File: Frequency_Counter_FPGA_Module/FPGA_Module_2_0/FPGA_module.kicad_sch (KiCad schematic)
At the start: 0 parts

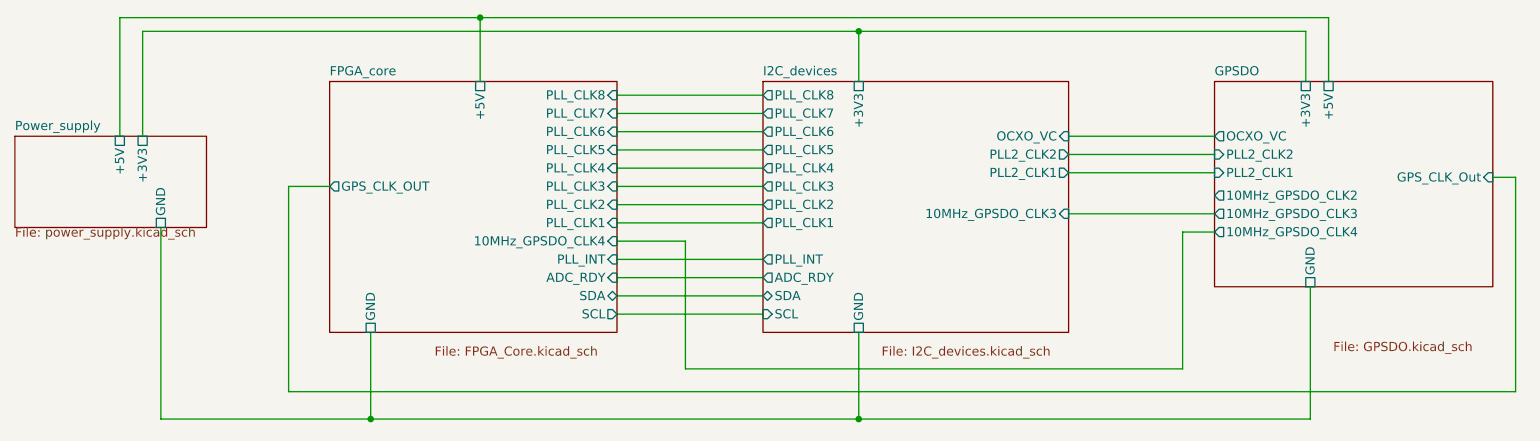
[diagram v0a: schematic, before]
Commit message: feat(boot): LED selftest blikaci kod + RTC LSE medium-low drive; UI 4.3" audit; FPGA HW revize
STM32H757 firmware:
- bootled.c/h: boot-time HW selftest diagnostika na LED_1 (PG3). Kazdy
  sledovany periferni init (FMC/SPI2/I2C4/DSIHOST/LTDC/USART1/RTC/ADC3/
  QUADSPI/I2C1) + display bring-up (panel probe/power-on/DSI start/
  TC358762) si zaznamena poradove cislo; pri zaseknuti v Error_Handler()
  LED bez displeje zabliká N-krat podle poradi. Regen-safe (jen chranene
  USER CODE hooky), bez zpozdeni v happy-path.
- RTC LSE Drive Capability LOW -> MEDIUM LOW (H757_LED.ioc): kompenzuje
  desky s predimenzovanymi zatezovymi kondenzatory krystalu (22pF misto
  18pF), ktere LSE nerozjizdely.
- UI audit pro realny 4,3" 800x480 panel (8,54 px/mm): hit-slop pilulek,
  fonty, HDR_PILL_LIMIT fit-check, Menu 3x4 mrizka s placeholdery, oprava
  ghost bugu AUTO CET/CEST tlacitka, sign-loss bug ve fmt_fixed/fmt_minmax.
  main-old layout zamrazen jako default (A/B srovnani, viz STATUS.md #14).

FPGA carrier v2.0 (KiCad): prubezne review checklisty a schema/PCB revize.

Co-Authored-By: OK2JNJ <ok2jnj@local>
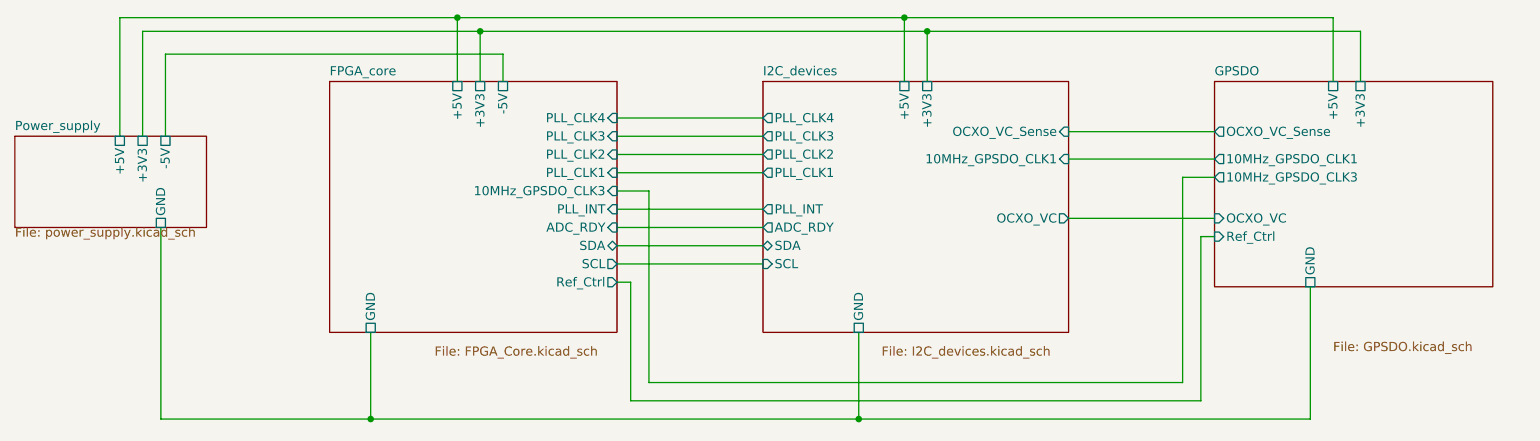
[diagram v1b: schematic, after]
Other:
- sheet FPGA_core ports: added +3V3, -5V, 10MHz_GPSDO_CLK3, Ref_Ctrl; removed 10MHz_GPSDO_CLK4, GPS_CLK_OUT, PLL_CLK5, PLL_CLK6, PLL_CLK7, PLL_CLK8
- sheet GPSDO ports: added 10MHz_GPSDO_CLK1, OCXO_VC_Sense, Ref_Ctrl; removed 10MHz_GPSDO_CLK2, 10MHz_GPSDO_CLK4, GPS_CLK_Out, PLL2_CLK1, PLL2_CLK2
- sheet I2C_devices ports: added +5V, 10MHz_GPSDO_CLK1, OCXO_VC_Sense; removed 10MHz_GPSDO_CLK3, PLL2_CLK1, PLL2_CLK2, PLL_CLK5, PLL_CLK6, PLL_CLK7, PLL_CLK8
- sheet Power_supply ports: added -5V; removed none

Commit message: feat(hw): FPGA carrier v2.0 — aktualizace schematu + PCB + checklist
KiCad FPGA_Module_2_0 (FPGA_Core/GPSDO/I2C_devices/power_supply schemata,
PCB layout, project), BOARD_V20_CHECKLIST.md. Odstranen zastaraly
FPGA_module_schematic.pdf (nahrazen exportem FPGA_module.pdf).

Co-Authored-By: OK2JNJ <ok2jnj@users.noreply.github.com>
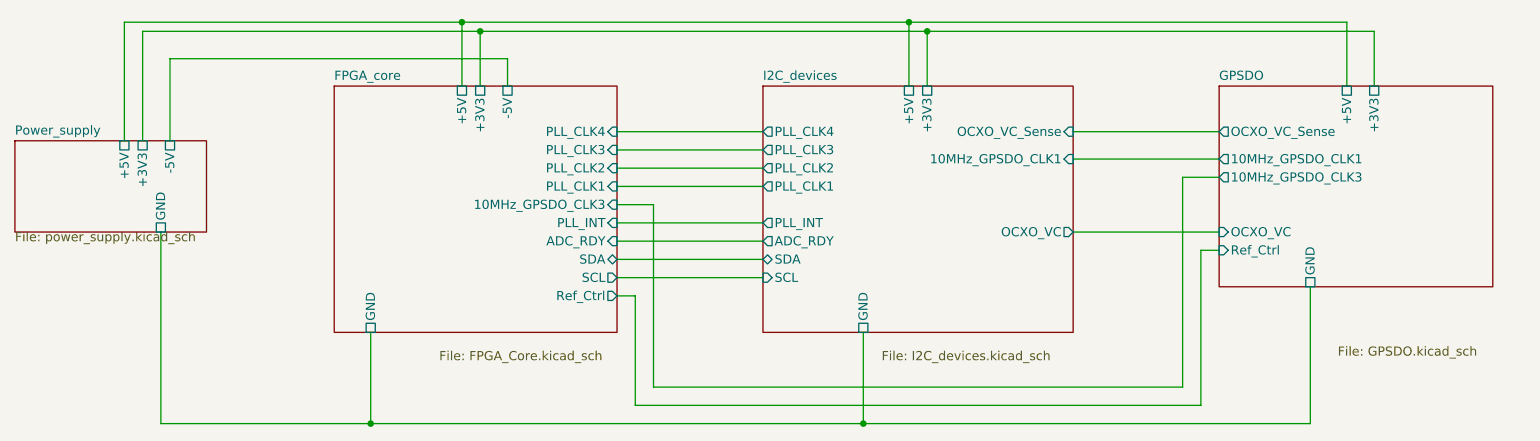
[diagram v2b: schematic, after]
